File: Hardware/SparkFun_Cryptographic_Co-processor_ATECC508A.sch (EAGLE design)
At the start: 22 parts, among them J1 QWIIC, J2 QWIIC, J3 PTH, U1 ATECC508A

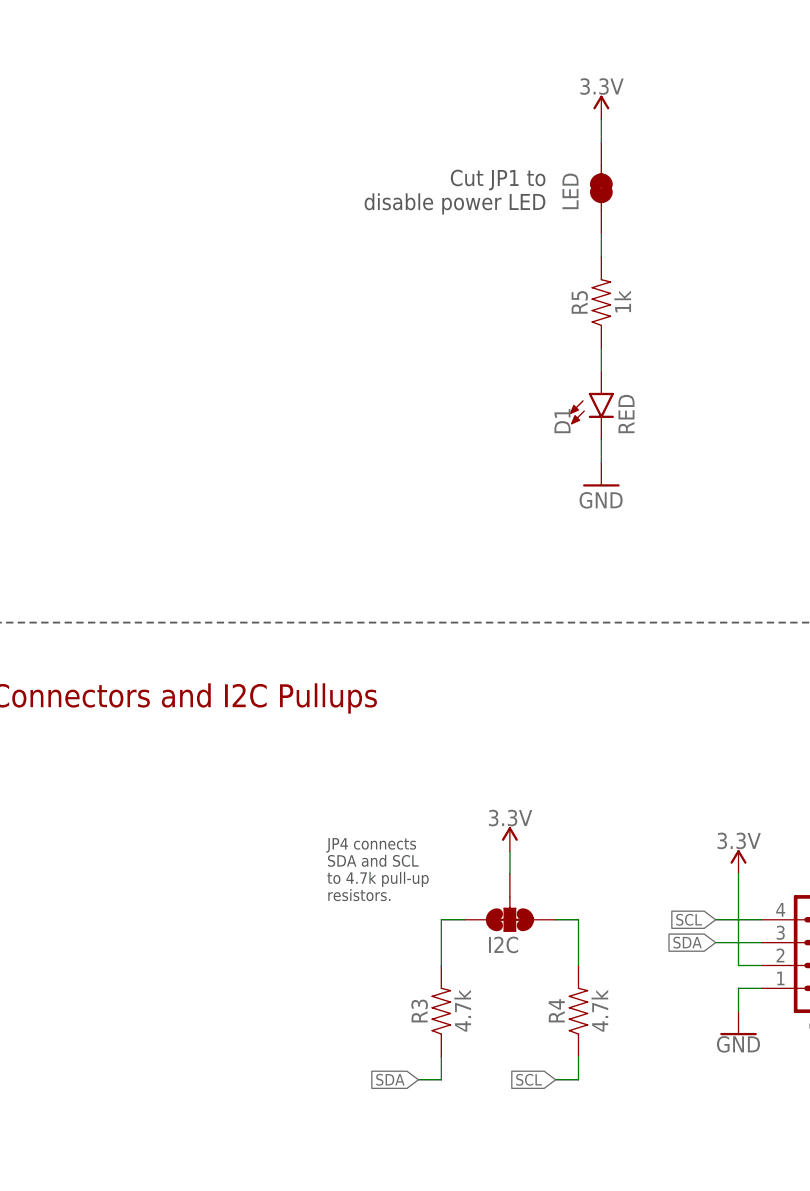
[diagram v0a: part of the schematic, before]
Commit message: swapped over to official SFE library for IC
added name and value to footprint.
removed local mini library.
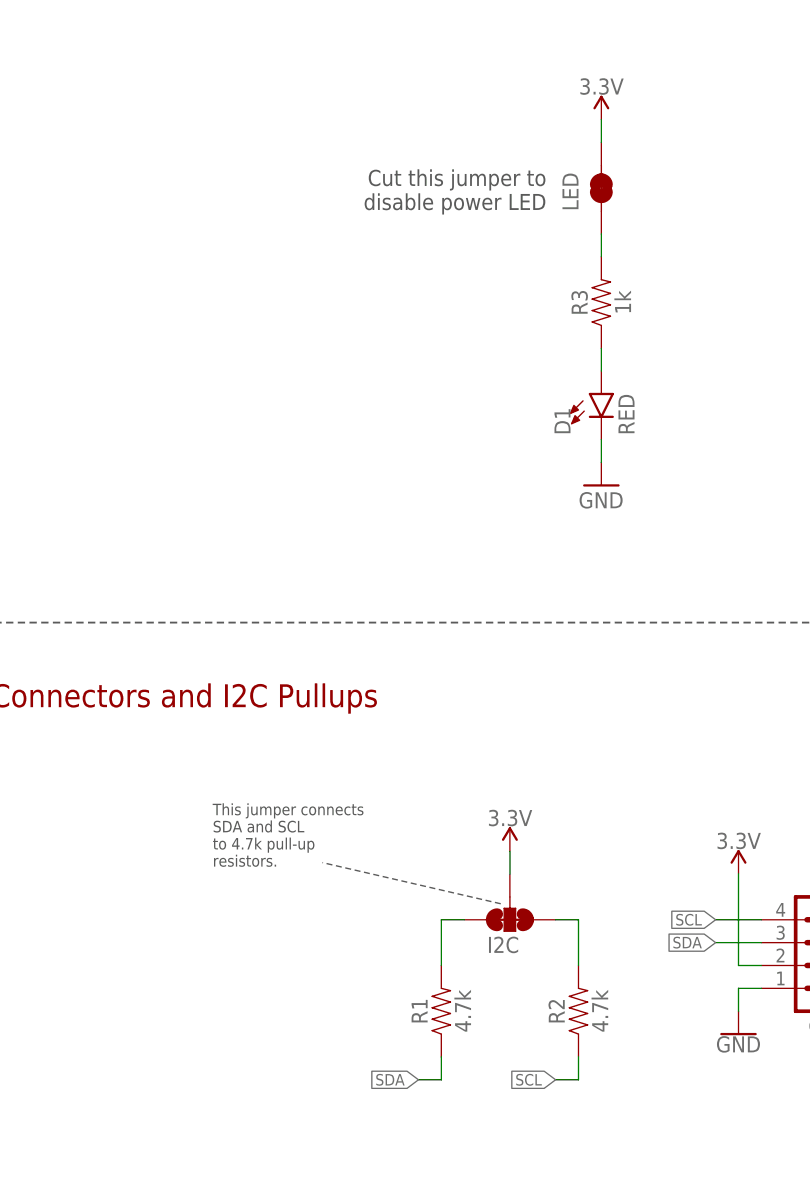
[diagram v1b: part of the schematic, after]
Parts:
- removed R5: 1k, SparkFun-Resistors:1KOHM-0603-1/10W-1%
- added R1: 4.7k, SparkFun-Resistors:4.7KOHM-0603-1/10W-1%
- R3: value 4.7k -> 1k; device SparkFun-Resistors:4.7KOHM-0603-1/10W-1% -> SparkFun-Resistors:1KOHM-0603-1/10W-1%
- U1: device ATECC508A:ATECC508AUDFN_2X3MM -> SparkFun-IC-Special-Function:ATECC508AUDFN_2X3MM
- renumbered R4 to R2
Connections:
- net N$3: now also R3.1; no longer R5.1
- net N$4: now also R1.2; no longer R3.2
- net N$7: now also R3.2; no longer R5.2
- net SDA: now also R1.1; no longer R3.1
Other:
- note added: "Cut this jumper to disable power LED"
- note added: "This jumper connects SDA and SCL to 4.7k pull-up resistors."
- note removed: "Cut JP1 to disable power LED"
- note removed: "JP4 connects SDA and SCL to 4.7k pull-up resistors."
- moved on the sheet: R3
